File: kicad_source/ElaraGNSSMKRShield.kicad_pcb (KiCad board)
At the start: 2 copper layers, 60 x 24 mm, 20 parts, among them CN1 ARDUINO_MKR, U1 TPS736XX, U2 WIRL-POSI_Elara-I, U3 PCA9306

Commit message: updated schematic and board
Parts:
- added C5: C_0603, capacitors:C_0603, F.Cu at (161.0, 135.3)
- added CN2: 60312202114509, CON_wuerth:WR-SMA-PCB, F.Cu at (174.0, 130.5)
- added D1: Led_Small, LEDs:LED_0603, F.Cu at (172.2, 139.2)
- added R13: 10k, resistors:R_0603, F.Cu at (143.0, 140.0)
- added R14: 1k, resistors:R_0603, F.Cu at (169.7, 139.2)
- added R15: 0R, resistors:R_0603, F.Cu at (166.9, 139.2)
- added R16: 0R, resistors:R_0603, F.Cu at (164.9, 139.2)
- added U4: SN74LVC2G34, SOT_TO:SOT-23-6, F.Cu at (161.0, 138.0)
- added W1: TEST_1P, wire_pads:SolderWirePad_single_1mmSMD, F.Cu at (134.5, 132.4)
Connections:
- CN1 pad 10: (no net) -> /1PPS
- CN1 pad 14: (no net) -> /ON_OFF
- CN1 pad 9: (no net) -> /WAKE_UP
- R1 pad 1: /ON_OFF -> /ON_OFF_1V8
- U2 pad 1: /ON_OFF -> /ON_OFF_1V8
- U2 pad 2: (no net) -> /1PPS_1V8
- U2 pad 6: (no net) -> /WAKE_UP_1V8
- U2 pad 8: (no net) -> /RESET
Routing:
- net /WAKE_UP_1V8: track 0.00 -> 54.3 mm, vias 0 -> 2
- net /1PPS_1V8: track 0.00 -> 47.7 mm, vias 0 -> 2
- net GND: track 85.0 -> 122.0 mm, vias 4 -> 17
- net /ON_OFF_1V8: track 0.00 -> 34.8 mm
- net /RESET: track 0.00 -> 25.9 mm, vias 0 -> 2
- net /1PPS_R: track 0.00 -> 18.9 mm
- net +3V3: track 53.2 -> 69.3 mm, vias 2 -> 4
- net /WAKE_UP: track 0.00 -> 10.6 mm
- net /1PPS: track 0.00 -> 10.6 mm
- net /WAKE_UP_R: track 0.00 -> 3.01 mm
- net Net-(D1-Pad2): track 0.00 -> 2.50 mm
- net /ON_OFF: track 28.8 -> 26.5 mm, vias 0 -> 1
- net /I2C_DAT: track 14.1 -> 13.5 mm
- net (no net): vias 8 -> 0
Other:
- board text added: "1PPS"

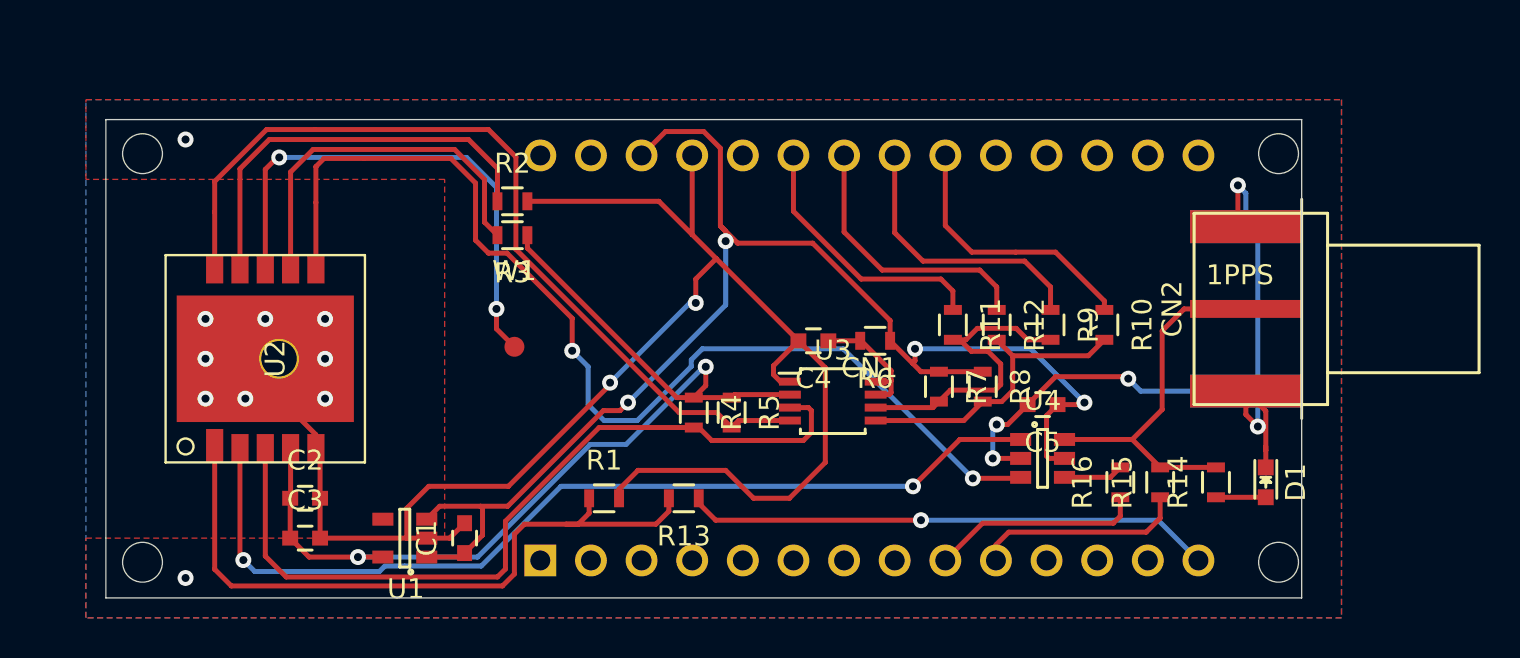
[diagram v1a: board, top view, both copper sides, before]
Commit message: updated level shifter circuit
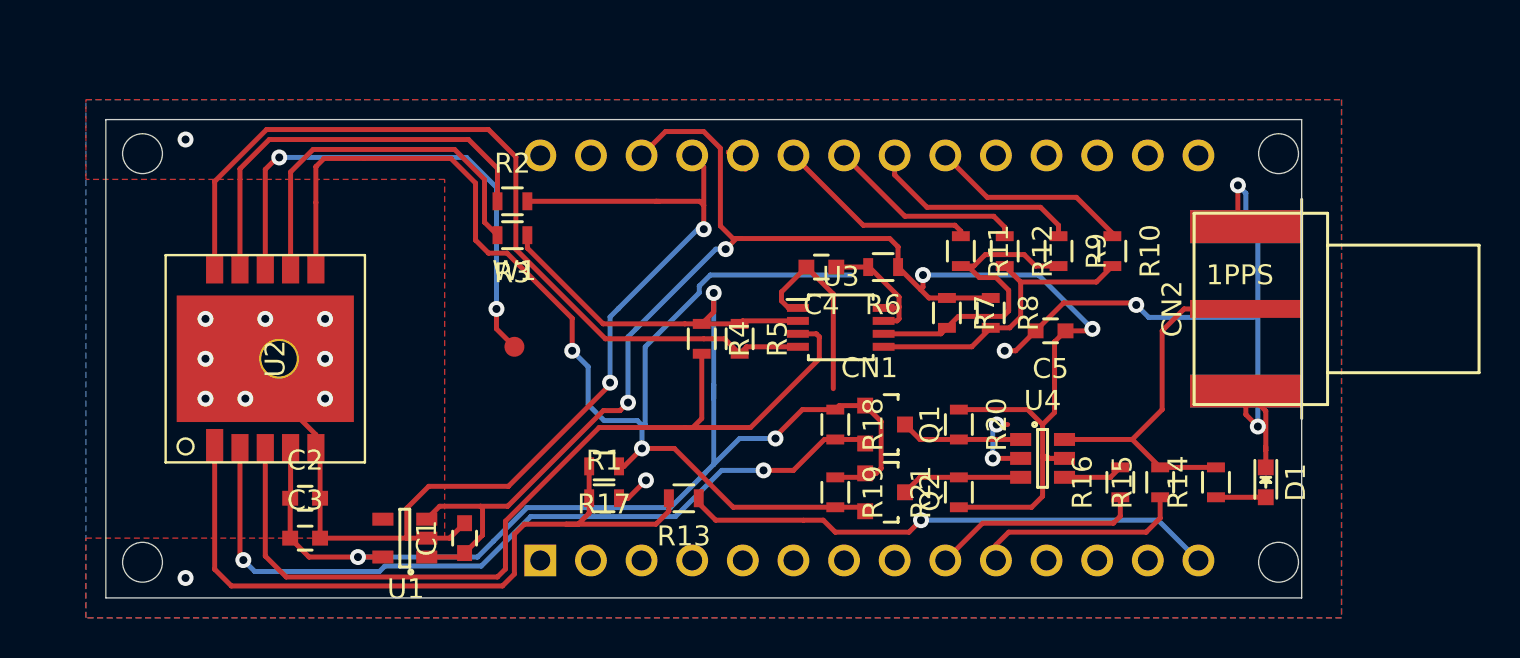
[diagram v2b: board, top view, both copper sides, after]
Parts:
- added Q1: BSS138, SOT_TO:SOT-23, F.Cu at (153.1, 136.3)
- added Q2: BSS138, SOT_TO:SOT-23, F.Cu at (153.1, 139.7)
- added R17: DNI, resistors:R_0603, F.Cu at (139.0, 138.4)
- added R18: 10k, resistors:R_0603, F.Cu at (150.6, 136.3)
- added R19: 10k, resistors:R_0603, F.Cu at (150.6, 139.7)
- added R20: 10k, resistors:R_0603, F.Cu at (156.8, 136.3)
- added R21: 10k, resistors:R_0603, F.Cu at (156.8, 139.7)
- moved C5 3.72 mm to (161.4, 131.6)
- moved R10 3.72 mm to (164.5, 127.6)
- moved R11 3.72 mm to (156.9, 127.6)
- moved R12 3.72 mm to (159.1, 127.6)
- moved R8 3.72 mm to (158.4, 130.7)
- moved R9 3.72 mm to (161.8, 127.6)
- moved R7 3.72 mm to (156.2, 130.7)
- moved C4 3.72 mm to (149.9, 128.4)
- moved R4 3.72 mm to (143.9, 132.0)
- moved R5 3.72 mm to (145.8, 132.0)
- moved R6 3.72 mm to (153.0, 128.4)
- moved U3 3.72 mm to (150.9, 131.4)
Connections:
- U4 pad 1: /1PPS_1V8 -> /1PPS_Q
- U4 pad 3: /WAKE_UP_1V8 -> /WAKE_UP_Q
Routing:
- net +1V8: track 49.8 -> 71.5 mm, vias 2 -> 3
- net GND: track 122.0 -> 105.6 mm, vias 17 -> 19
- net +3V3: track 69.3 -> 84.8 mm
- net /WAKE_UP_1V8: track 54.3 -> 62.4 mm
- net /1PPS_1V8: track 47.7 -> 39.9 mm
- net /WAKE_UP_Q: track 0.00 -> 6.11 mm
- net /1PPS_Q: track 0.00 -> 6.11 mm
- net /I2C_CLK_1V8: track 40.4 -> 45.7 mm
- net /RX: track 13.8 -> 10.0 mm
- net /I2C_DAT: track 13.5 -> 10.1 mm
- net /I2C_CLK: track 14.0 -> 10.8 mm
- net /TX: track 13.4 -> 10.2 mm
- net /ON_OFF_1V8: track 34.8 -> 36.4 mm
- net (no net): track 0.00 -> 1.60 mm
- net /I2C_DAT_1V8: track 43.4 -> 42.3 mm

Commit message: beautified layout, added images, updated files
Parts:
- added L1: Label, labels:generationmake_small_solder, F.Cu at (139.5, 128.6)
- CN1: footprint MODULE_compute:ARDUINO_MKR_HOLES -> MODULE_compute:ARDUINO_MKR_HOLES_PINHEADER
- moved C1 8.57 mm to (129.5, 133.8), turned to 180 degrees
- moved C3 6.26 mm to (129.5, 139.0), turned to 180 degrees
- moved R3 6.08 mm to (129.5, 123.2), turned to 90 degrees
- moved U1 5.62 mm to (129.5, 136.4), turned to 270 degrees
- moved C2 5.14 mm to (119.9, 136.9)
- moved U2 5.00 mm to (118.0, 130.0)
- moved R13 4.81 mm to (139.7, 136.5), turned to 270 degrees
- moved R1 4.55 mm to (136.1, 136.5), turned to 90 degrees
- moved C4 3.75 mm to (147.6, 125.4)
- moved CN1 3.75 mm to (150.0, 130.0)
- moved Q1 3.75 mm to (150.8, 133.3)
- moved R18 3.75 mm to (148.3, 133.3)
- moved R20 3.75 mm to (154.5, 133.3)
- moved R4 3.75 mm to (141.6, 129.0)
- moved R5 3.75 mm to (143.5, 129.0)
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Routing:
- net GND: track 105.6 -> 77.0 mm, vias 19 -> 23
- net +3V3: track 84.8 -> 69.7 mm, vias 4 -> 3
- net /WAKE_UP_1V8: track 62.4 -> 52.9 mm
- net /ON_OFF_1V8: track 36.4 -> 31.6 mm
- net /I2C_CLK_TX: track 16.1 -> 11.3 mm
- net /ON_OFF: track 27.0 -> 29.2 mm
- net /I2C_CLK_1V8: track 45.7 -> 43.9 mm
- net /I2C_DAT_RX: track 15.3 -> 13.5 mm
- net /RESET: track 25.9 -> 27.6 mm
- net /I2C_DAT_1V8: track 42.3 -> 44.0 mm
- net /I2C_DAT: track 10.1 -> 11.6 mm
- net /CTS: track 18.8 -> 17.7 mm
- net /RTS: track 20.8 -> 21.6 mm
- net /1PPS: track 10.6 -> 10.0 mm
- net /I2C_CLK: track 10.8 -> 11.4 mm
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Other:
- board text added: "0.1"
- board text added: "ElaraGNSSMKRShield"
- board text added: "I2C"
- board text added: "RESET"
- board text added: "bot"
- board text added: "serial"
- board text added: "top"

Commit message: added wuerth part numbers
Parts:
- added L2: Label, labels:generationmake_logo, B.Cu at (167.8, 103.0)
- C1, C2, C3, C5: value C_0603 -> 885012206095
- C4: value 100pF -> 885012206077
- D1: value Led_Small -> 150060GS75000
- R3: value 10k -> DNI
- U1: value TPS736XX -> TPS73618DBV
- U2: value WIRL-POSI_Elara-I -> 2613011037000

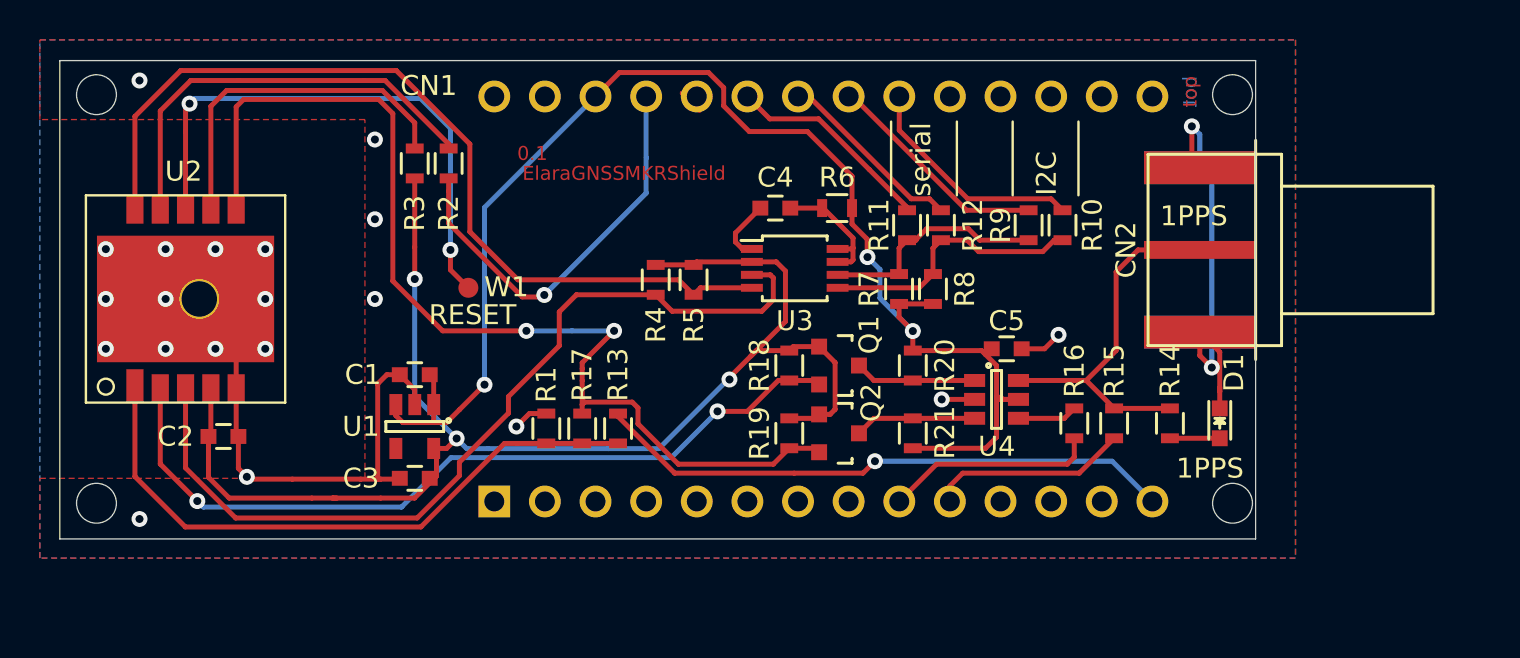
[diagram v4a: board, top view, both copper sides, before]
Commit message: updated shape of PCB
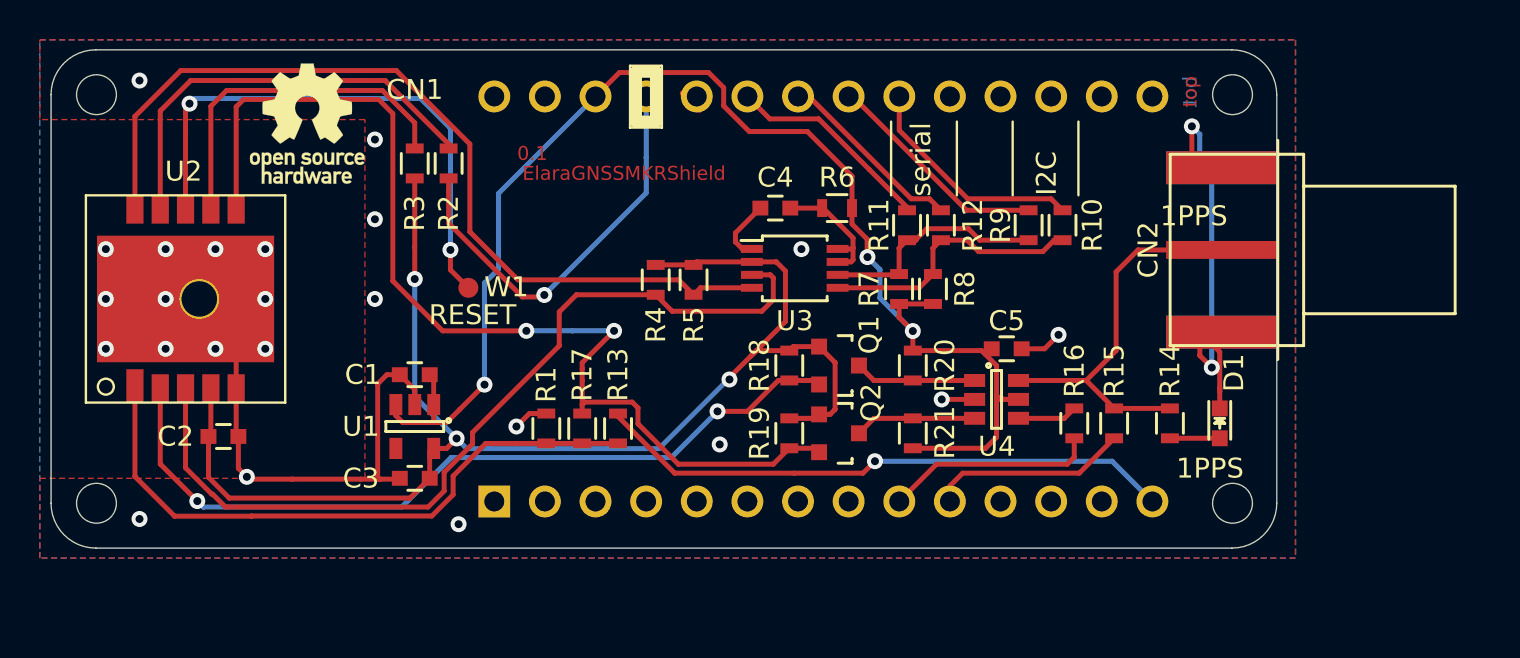
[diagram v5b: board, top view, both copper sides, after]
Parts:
- added L3: Label, Symbol:OSHW-Logo_5.7x6mm_SilkScreen, F.Cu at (124.1, 121.2)
- CN1: footprint MODULE_compute:ARDUINO_MKR_HOLES_PINHEADER -> MODULE_compute:ARDUINO_MKR_HOLES_PINHEADER_EDGE
- moved L2 35.6 mm to (145.5, 130.8), turned to 180 degrees
- moved CN2 1.11 mm to (172.8, 127.5)
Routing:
- net GND: vias 23 -> 26
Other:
- board size 60 x 24 mm -> 61.5 x 25 mm
- board text added: "Licensed under CERN OHL v.1.2"
